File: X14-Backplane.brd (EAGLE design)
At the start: 88.9 x 139.7 mm, 34 parts, among them J2 PXC-PTSM-04-RA-1778641, J3 PXC-8-RA-1778683, J8 PXC-8-RA-1778683

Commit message: STEPS!
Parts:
- DIST_TO_BACKPLANE: device Samtec MPPT Hermaphoditic 10 pos - MPPT-10-01-01-L-RA-SD:MPPT-10-01-01-L-RA-SD -> CONN, Samtec MPPT Hermaphoditic 10 pos - MPPT-10-01-01-L-RA-SD:MPPT-10-01-01-L-RA-SD
- J2: device Phoenix Contact PTSM-04-V-1778573:PXC-PTSM-04-RA-1778641 -> CONN, Phoenix Contact PTSM-04-V-1778573:PXC-PTSM-04-RA-1778641
- J3, J8: device Phoenix Contact PTSM 8 pin:PXC-8-RA-1778683 -> CONN, Phoenix Contact PTSM 8 pin:PXC-8-RA-1778683
- U$1, U$2, U$3: device BLHeli_32 45A:BACKPLANE_CONNECTORS_BKP -> Conn, Backplane-ESC-Controller:BACKPLANE_CONNECTORS_BKP
- U$5, U$6, U$7: device Backplane_ESC_adapter:BACKPLANE_ESC_ADAPTER_BKP_PWR -> CONN, Backplane_ESC_adapter:BACKPLANE_ESC_ADAPTER_BKP_PWR
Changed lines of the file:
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@@
 <attribute name="VALUE" x="65.532" y="113.03" size="0.6096" layer="27" font="vector" ratio="20" align="top-center"/>
 </element>
-<element name="DIST_TO_BACKPLANE" library="Samtec MPPT Hermaphoditic 10 pos - MPPT-10-01-01-L-RA-SD" package="MPPT-10-01-01-L-RA-SD" package3d_urn="urn:adsk.eagle:package:25115828/2" value="" x="43.18" y="139.7" smashed="yes" rot="R180">
+<element name="DIST_TO_BACKPLANE" library="CONN, Samtec MPPT Hermaphoditic 10 pos - MPPT-10-01-01-L-RA-SD" package="MPPT-10-01-01-L-RA-SD" package3d_urn="urn:adsk.eagle:package:25115828/2" value="" x="43.18" y="139.7" smashed="yes" rot="R180">
 <attribute name="NAME" x="60.96" y="139.7" size="1.27" layer="25" rot="R180" align="bottom-center"/>
 </element>
@@
 <attribute name="VALUE" x="85.09" y="1.524" size="0.6096" layer="28" font="vector" ratio="20" rot="MR0" align="top-center"/>
 </element>
-<element name="J2" library="Phoenix Contact PTSM-04-V-1778573" package="PXC-PTSM-04-RA-1778641" value="PXC-PTSM-04-RA-1778641" x="2.032" y="51.308" smashed="yes" rot="R270">
+<element name="J2" library="CONN, Phoenix Contact PTSM-04-V-1778573" package="PXC-PTSM-04-RA-1778641" package3d_urn="urn:adsk.eagle:package:33723680/2" value="PXC-PTSM-04-RA-1778641" x="2.032" y="51.308" smashed="yes" rot="R270">
 <attribute name="NAME" x="-2.714" y="51.308" size="1.27" layer="25" rot="R270"/>
 </element>
-<element name="J3" library="Phoenix Contact PTSM 8 pin" package="PXC-8-RA-1778683" package3d_urn="urn:adsk.eagle:package:25224885/2" value="PXC-8-RA-1778683" x="-3.81" y="125.222" smashed="yes" rot="R270"/>
+<element name="J3" library="CONN, Phoenix Contact PTSM 8 pin" package="PXC-8-RA-1778683" package3d_urn="urn:adsk.eagle:package:25224885/2" value="PXC-8-RA-1778683" x="-3.81" y="125.222" smashed="yes" rot="R270"/>
 <element name="MUX" library="BackplaneMUX" package="SOIC-16" value="TI-SN74LV4052A" x="23.876" y="116.586" smashed="yes" rot="R180">
 <attribute name="NAME" x="17.276" y="126.286" size="1.27" layer="25"/>
@@
 <attribute name="VALUE" x="2.794" y="89.408" size="0.6096" layer="27" font="vector" ratio="20" rot="R270" align="top-center"/>
 </element>
-<element name="U$1" library="BLHeli_32 45A" package="BACKPLANE_CONNECTORS_BKP" value="BACKPLANE_CONNECTORSBKP" x="17.78" y="108.204" smashed="yes" rot="R180"/>
-<element name="U$2" library="BLHeli_32 45A" package="BACKPLANE_CONNECTORS_BKP" value="BACKPLANE_CONNECTORSBKP" x="17.526" y="64.77" smashed="yes" rot="R180"/>
-<element name="U$3" library="BLHeli_32 45A" package="BACKPLANE_CONNECTORS_BKP" value="BACKPLANE_CONNECTORSBKP" x="17.526" y="21.336" smashed="yes" rot="R180"/>
-<element name="U$5" library="Backplane_ESC_adapter" package="BACKPLANE_ESC_ADAPTER_BKP_PWR" value="BACKPLANE_ESC_ADAPTER_PWRBKP" x="95.25" y="137.414" smashed="yes" rot="R180">
+<element name="U$1" library="Conn, Backplane-ESC-Controller" package="BACKPLANE_CONNECTORS_BKP" package3d_urn="urn:adsk.eagle:package:33721620/2" value="BACKPLANE_CONNECTORSBKP" x="17.78" y="108.204" smashed="yes" rot="R180"/>
+<element name="U$2" library="Conn, Backplane-ESC-Controller" package="BACKPLANE_CONNECTORS_BKP" package3d_urn="urn:adsk.eagle:package:33721620/2" value="BACKPLANE_CONNECTORSBKP" x="17.526" y="64.77" smashed="yes" rot="R180"/>
+<element name="U$3" library="Conn, Backplane-ESC-Controller" package="BACKPLANE_CONNECTORS_BKP" package3d_urn="urn:adsk.eagle:package:33721620/2" value="BACKPLANE_CONNECTORSBKP" x="17.526" y="21.336" smashed="yes" rot="R180"/>
+<element name="U$5" library="CONN, Backplane_ESC_adapter" package="BACKPLANE_ESC_ADAPTER_BKP_PWR" package3d_urn="urn:adsk.eagle:package:33723362/2" value="BACKPLANE_ESC_ADAPTER_PWRBKP" x="95.25" y="137.414" smashed="yes" rot="R180">
 <attribute name="NAME" x="58.42" y="104.775" size="1.27" layer="25" rot="R180"/>
 </element>
-<element name="U$6" library="Backplane_ESC_adapter" package="BACKPLANE_ESC_ADAPTER_BKP_PWR" value="BACKPLANE_ESC_ADAPTER_PWRBKP" x="95.25" y="95.25" smashed="yes" rot="R180">
+<element name="U$6" library="CONN, Backplane_ESC_adapter" package="BACKPLANE_ESC_ADAPTER_BKP_PWR" package3d_urn="urn:adsk.eagle:package:33723362/2" value="BACKPLANE_ESC_ADAPTER_PWRBKP" x="95.25" y="95.25" smashed="yes" rot="R180">
 <attribute name="NAME" x="58.42" y="62.611" size="1.27" layer="25" rot="R180"/>
 </element>
-<element name="U$7" library="Backplane_ESC_adapter" package="BACKPLANE_ESC_ADAPTER_BKP_PWR" value="BACKPLANE_ESC_ADAPTER_PWRBKP" x="95.25" y="52.832" smashed="yes" rot="R180">
+<element name="U$7" library="CONN, Backplane_ESC_adapter" package="BACKPLANE_ESC_ADAPTER_BKP_PWR" package3d_urn="urn:adsk.eagle:package:33723362/2" value="BACKPLANE_ESC_ADAPTER_PWRBKP" x="95.25" y="52.832" smashed="yes" rot="R180">
 <attribute name="NAME" x="58.42" y="20.193" size="1.27" layer="25" rot="R180"/>
 </element>
@@
 <attribute name="VALUE" x="1.651" y="97.028" size="1.27" layer="27" rot="R270" align="top-center"/>
 </element>
-<element name="U$4" library="CONN, Distribution-Backplane" package="SAMTEC_IPL1-107-01-X-D-K(B-D)" value="BACKPLANE-DISTRIBUTION" x="81.788" y="123.952" smashed="yes" rot="R90">
+<element name="U$4" library="CONN, Distribution-Backplane" package="SAMTEC_IPL1-107-01-X-D-K(B-D)" package3d_urn="urn:adsk.eagle:package:32878650/2" value="BACKPLANE-DISTRIBUTION" x="81.788" y="123.952" smashed="yes" rot="R90">
 <attribute name="NAME" x="78.478" y="115.462" size="1.778" layer="25" rot="R90"/>
 </element>
-<element name="J8" library="Phoenix Contact PTSM 8 pin" package="PXC-8-RA-1778683" package3d_urn="urn:adsk.eagle:package:25224885/2" value="PXC-8-RA-1778683" x="92.964" y="61.976" smashed="yes" rot="R90"/>
-<element name="U$9" library="PI-SHIELD, Solenoid-Backplane" package="IPL7X2" value="7X_CONN" x="80.772" y="36.576" smashed="yes" rot="R270"/>
-<element name="U$10" library="CONN, DataConversion-Backplane Connector- SAMTEC CLT-107-01-F-D" package="SAMTEC-CLT-107-01-X-D-BACKPLANE" value="BACKPLANE-&gt;DATACONV" x="69.088" y="121.92" smashed="yes">
+<element name="J8" library="CONN, Phoenix Contact PTSM 8 pin" package="PXC-8-RA-1778683" package3d_urn="urn:adsk.eagle:package:25224885/2" value="PXC-8-RA-1778683" x="92.964" y="61.976" smashed="yes" rot="R90"/>
+<element name="U$9" library="PI-SHIELD, Solenoid-Backplane" package="IPL7X2" package3d_urn="urn:adsk.eagle:package:33723615/2" value="7X_CONN" x="80.772" y="36.576" smashed="yes" rot="R270"/>
+<element name="U$10" library="CONN, DataConversion-Backplane Connector- SAMTEC CLT-107-01-F-D" package="SAMTEC-CLT-107-01-X-D-BACKPLANE" package3d_urn="urn:adsk.eagle:package:33723582/2" value="BACKPLANE-&gt;DATACONV" x="69.088" y="121.92" smashed="yes">
 <attribute name="NAME" x="62.173" y="125.237" size="1.016" layer="25"/>
 </element>

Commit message: new connector UwU SQT
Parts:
- removed U$1, U$2, U$3: BACKPLANE_CONNECTORSBKP, Conn, Backplane-ESC-Controller:BACKPLANE_CONNECTORS_BKP
- added U$11, U$12, U$13: BACKPLANE_ESC, SQT-106-01-F-D:SAMTEC_SQT-107-01-F-D
- moved R4 1.55 mm to (18.3, 99.6), turned to 180 degrees
- moved R5 1.08 mm to (17.3, 13.0), turned to 180 degrees
- moved R1 0.80 mm to (17.3, 56.1), turned to 180 degrees
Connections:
- net 3V3: now also U$11.01, U$11.02, U$11.03, U$11.04, U$12.01, U$12.02, U$12.03, U$12.04, U$13.01, U$13.02, U$13.03, U$13.04; no longer U$1.1, U$1.2, U$1.3, U$1.4, U$2.1, U$2.2, U$2.3, U$2.4, U$3.1, U$3.2, U$3.3, U$3.4
- net CAN_H: now also U$11.05, U$12.05, U$13.05; no longer U$1.5, U$2.5, U$3.5
- net CAN_L: now also U$11.07, U$12.07, U$13.07; no longer U$1.7, U$2.7, U$3.7
- net ESCID_1: now also U$11.12; no longer U$1.12
- net ESCID_2: now also U$13.12; no longer U$2.12
- net ESCID_3: now also U$12.12; no longer U$3.12
- net GND_L: now also U$11.10, U$12.10, U$13.10; no longer U$1.10, U$2.10, U$3.10
- net NRST_1: now also U$11.06; no longer U$1.6
- net NRST_2: now also U$13.06; no longer U$2.6
- net NRST_3: now also U$12.06; no longer U$3.6
- net SWCLK_1: now also U$11.11; no longer U$1.11
- net SWCLK_2: now also U$13.11; no longer U$2.11
- net SWCLK_3: now also U$12.11; no longer U$3.11
- net SWDIO_1: now also U$11.09; no longer U$1.9
- net SWDIO_2: now also U$13.09; no longer U$2.9
- net SWDIO_3: now also U$12.09; no longer U$3.9
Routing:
- net 3V3: track 436.6 -> 424.5 mm
- net ESCID_1: track 3.05 -> 3.91 mm
- net ESCID_2: track 3.05 -> 3.68 mm

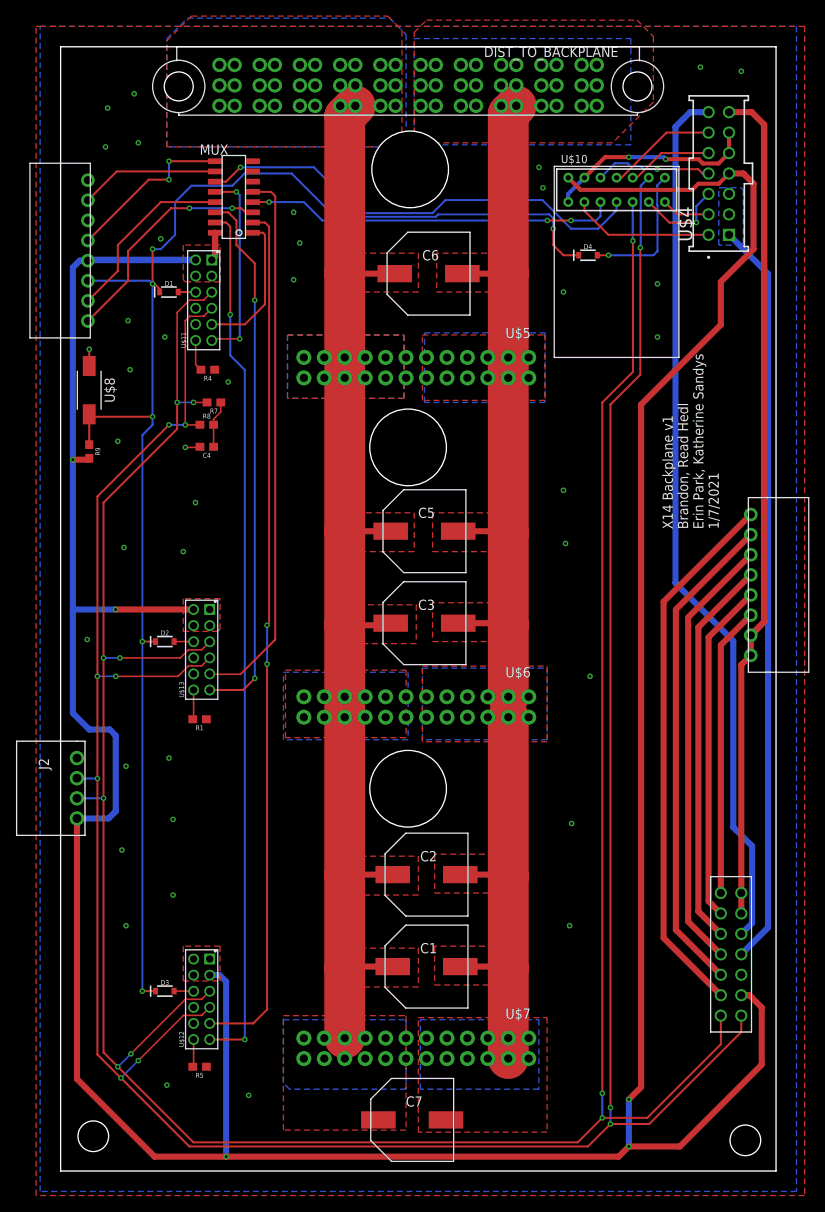
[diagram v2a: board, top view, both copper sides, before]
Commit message: shrunk board to better fit in box for v2
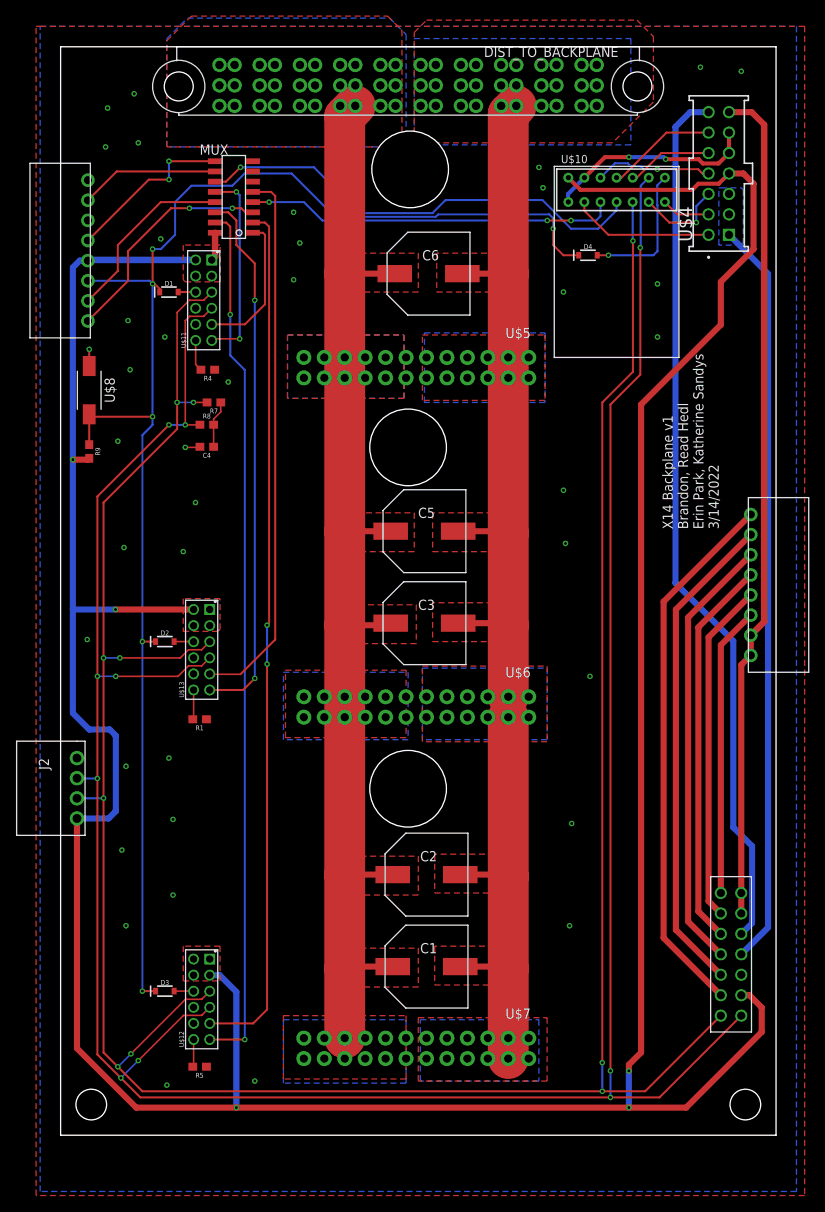
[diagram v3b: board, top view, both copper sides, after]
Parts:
- removed C7: 330uF, CAP, aluminin-capacitor-brick-UCM1H331MNL1GS:CAPAE1030X1050N
- moved H2 4.45 mm to (85.1, 8.26)
- moved H1 3.95 mm to (3.81, 8.26)
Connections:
- net 12V: no longer C7.+
- net 12VGND: no longer C7.-
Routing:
- net 3V3: track 424.5 -> 404.4 mm
- net CAN_H: track 342.8 -> 332.1 mm
- net CAN_L: track 347.0 -> 337.5 mm
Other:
- board size 88.9 x 139.7 mm -> 88.9 x 135.3 mm
- board text added: "X14 Backplane v1 Brandon, Read Hedl Erin Park, Katherine Sandys 3/14/2022"
- board text removed: "X14 Backplane v1 Brandon, Read Hedl Erin Park, Katherine Sandys 1/7/2021"
